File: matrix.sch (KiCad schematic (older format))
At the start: 139 parts

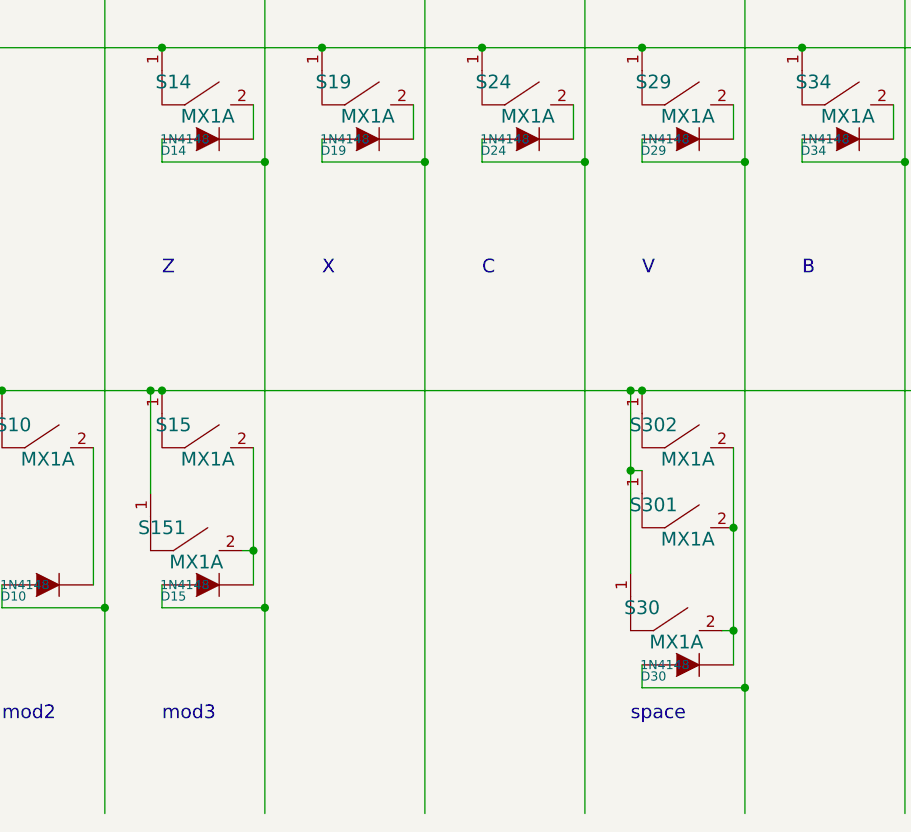
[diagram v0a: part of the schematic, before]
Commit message: Remove unnecessary related SWs to SW30
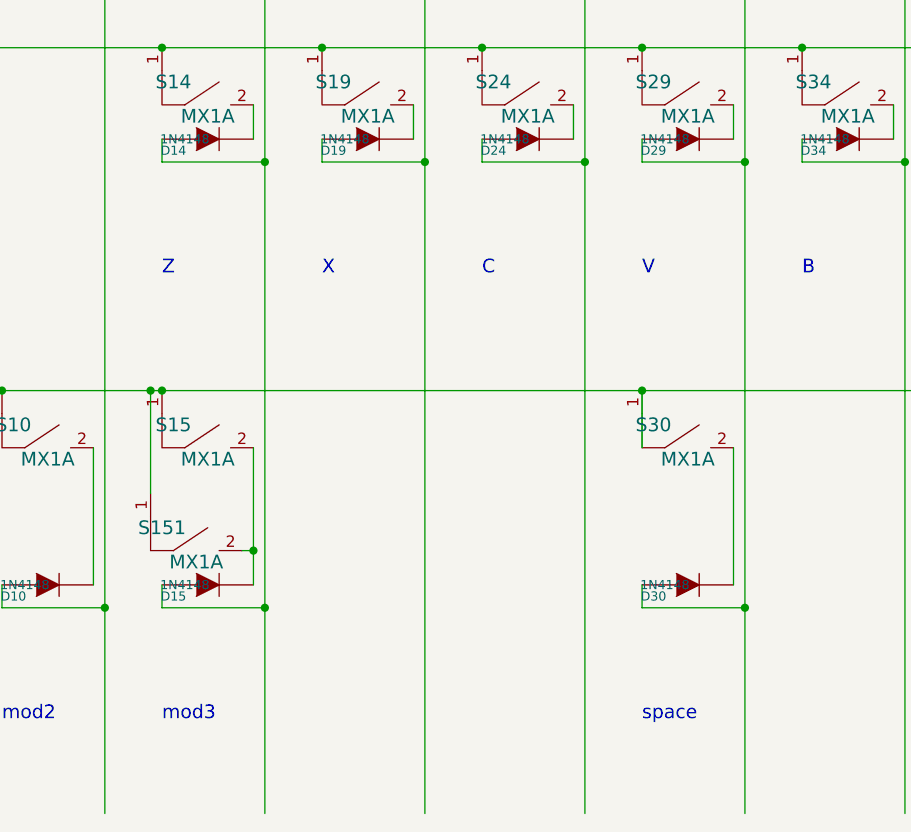
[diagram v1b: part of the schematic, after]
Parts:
- removed S301, S302: MX1A, mx1a:MX1A_no3d, symbol mx1a-simple:MX1A
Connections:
- wire segments 383 -> 377
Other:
- moved on the sheet: D30, S30
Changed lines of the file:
@@
-$EndComp
-$Comp
-L mx1a-simple:MX1A S301
-U 1 1 5040FAEC
-P 6850 8900
-F 0 "S301" H 6700 9150 60  0000 C CNN
-F 1 "MX1A" H 6850 9000 60  0000 C CNN
-F 2 "mx1a:MX1A_no3d" H 6850 8900 60  0001 C CNN
-F 3 "" H 6850 8900 60  0001 C CNN
-	1    6850 8900
-	1    0    0    -1
-$EndComp
-$Comp
-L mx1a-simple:MX1A S302
-U 1 1 5040FAF4
-P 6850 8550
-F 0 "S302" H 6700 8800 60  0000 C CNN
-F 1 "MX1A" H 6850 8650 60  0000 C CNN
-F 2 "mx1a:MX1A_no3d" H 6850 8550 60  0001 C CNN
-F 3 "" H 6850 8550 60  0001 C CNN
-	1    6850 8550
-	1    0    0    -1
 $EndComp
 $Comp
@@
 L mx1a-simple:MX1A S30
 U 1 1 5040DF35
-P 6800 9350
-F 0 "S30" H 6650 9600 60  0000 C CNN
-F 1 "MX1A" H 6800 9450 60  0000 C CNN
-F 2 "mx1a:MX1A" H 6800 9350 60  0001 C CNN
-F 3 "" H 6800 9350 60  0001 C CNN
-	1    6800 9350
+P 6850 8550
+F 0 "S30" H 6700 8800 60  0000 C CNN
+F 1 "MX1A" H 6850 8650 60  0000 C CNN
+F 2 "mx1a:MX1A" H 6850 8550 60  0001 C CNN
+F 3 "" H 6850 8550 60  0001 C CNN
+	1    6850 8550
 	1    0    0    -1
 $EndComp
@@
 L device:DIODE D30
 U 1 1 506B5D8C
-P 6850 9350
-F 0 "D30" H 6700 9300 40  0000 C CNN
-F 1 "1N4148" H 6750 9350 40  0000 C CNN
-F 2 "0805:0805D" H 6850 9350 60  0001 C CNN
-F 3 "" H 6850 9350 60  0001 C CNN
-F 4 "DC Components" H 4100 5050 60  0001 C CNN "Vendor"
-F 5 "CD4148WS(0805C)" H 4100 5050 60  0001 C CNN "Product"
-F 6 "TME" H 4100 5050 60  0001 C CNN "Supplier"
-F 7 "1N4148-0805" H 4100 5050 60  0001 C CNN "Supplier Symbol"
-	1    6850 9350
+P 6850 9000
+F 0 "D30" H 6700 8950 40  0000 C CNN
+F 1 "1N4148" H 6750 9000 40  0000 C CNN
+F 2 "0805:0805D" H 6850 9000 60  0001 C CNN
+F 3 "" H 6850 9000 60  0001 C CNN
+F 4 "DC Components" H 4100 4700 60  0001 C CNN "Vendor"
+F 5 "CD4148WS(0805C)" H 4100 4700 60  0001 C CNN "Product"
+F 6 "TME" H 4100 4700 60  0001 C CNN "Supplier"
+F 7 "1N4148-0805" H 4100 4700 60  0001 C CNN "Supplier Symbol"
+	1    6850 9000
 	1    0    0    -1
 $EndComp
@@
 Text Notes 4550 9600 0    60   ~ 0
 mod3
-Text Notes 6600 9600 0    60   ~ 0
-space
 Text Notes 10100 9600 0    60   ~ 0
 mod4
@@
 	11250 8400 11250 8700
 Wire Wire Line
-	7050 8400 7050 8750
-Wire Wire Line
 	12650 8400 12650 8850
 Wire Wire Line
@@
 Connection ~ 12200 5150
 Wire Wire Line
-	6600 8150 6600 8500
-Connection ~ 6600 8150
-Wire Wire Line
 	10550 8850 10500 8850
 Wire Wire Line
@@
 Wire Wire Line
 	12650 8850 12600 8850
-Wire Wire Line
-	7050 9200 7000 9200
 Wire Wire Line
 	12200 6650 12200 7100
@@
 Connection ~ 5950 5150
 Connection ~ 5950 6650
-Connection ~ 6650 8150
 Connection ~ 8750 2950
 Connection ~ 8050 2950
@@
 Wire Wire Line
 	4550 9000 4550 9100
-Wire Wire Line
-	6650 9350 6650 9450
-Wire Wire Line
-	6650 9450 7100 9450
 Connection ~ 12650 8850
 Connection ~ 11950 8850
 Connection ~ 10550 8850
 Connection ~ 11250 9150
-Connection ~ 7050 9200
 Wire Wire Line
 	3150 5550 3150 5650
@@
 Connection ~ 6400 7150
 Connection ~ 5700 7150
-Connection ~ 7100 9450
 Connection ~ 9200 3450
 Connection ~ 9900 3450
@@
 Wire Wire Line
 	12250 3450 12250 3350
-Connection ~ 7050 8750
-Wire Wire Line
-	6650 8500 6600 8500
-Connection ~ 6600 8500
 Wire Wire Line
 	12600 7350 12650 7350
@@
 	10150 8150 10800 8150
 Wire Wire Line
-	4550 8150 6600 8150
-Wire Wire Line
 	12250 6650 13250 6650
 Wire Wire Line
@@
 	12200 5150 12250 5150
 Wire Wire Line
-	6600 8150 6650 8150
-Wire Wire Line
 	12200 6650 12250 6650
 Wire Wire Line
@@
 	11250 9150 11250 9300
 Wire Wire Line
-	7050 9200 7050 9350
-Wire Wire Line
 	3600 3450 3600 4650
 Wire Wire Line
@@
 	7800 7150 7800 10000
 Wire Wire Line
-	7100 7150 7100 9450
-Wire Wire Line
 	6400 7150 6400 10000
 Wire Wire Line
 	5700 7150 5700 10000
 Wire Wire Line
-	7100 9450 7100 10000
-Wire Wire Line
 	9200 3450 9200 4650
 Wire Wire Line
@@
 	12650 7500 12650 7650
 Wire Wire Line
-	7050 8750 7050 9200
-Wire Wire Line
-	6600 8500 6600 8950
-Wire Wire Line
 	12650 7350 12650 7500
 Wire Wire Line
 	12200 7100 12200 7250
-Wire Wire Line
-	6650 8150 10100 8150
 Wire Wire Line
 	9900 7150 9900 10000
@@
 Wire Wire Line
 	3600 5650 3600 7450
+Wire Wire Line
+	7050 8400 7050 9000
+Wire Wire Line
+	6650 8150 6650 8400
+Wire Wire Line
+	7100 7150 7100 9100
+Connection ~ 6650 8150
+Wire Wire Line
+	6650 8150 10100 8150
+Wire Wire Line
+	4550 8150 6650 8150
+Wire Wire Line
+	6650 9000 6650 9100
+Wire Wire Line
+	6650 9100 7100 9100
+Connection ~ 7100 9100
+Wire Wire Line
+	7100 9100 7100 10000
+Text Notes 6650 9600 0    60   ~ 0
+space
 $EndSCHEMATC

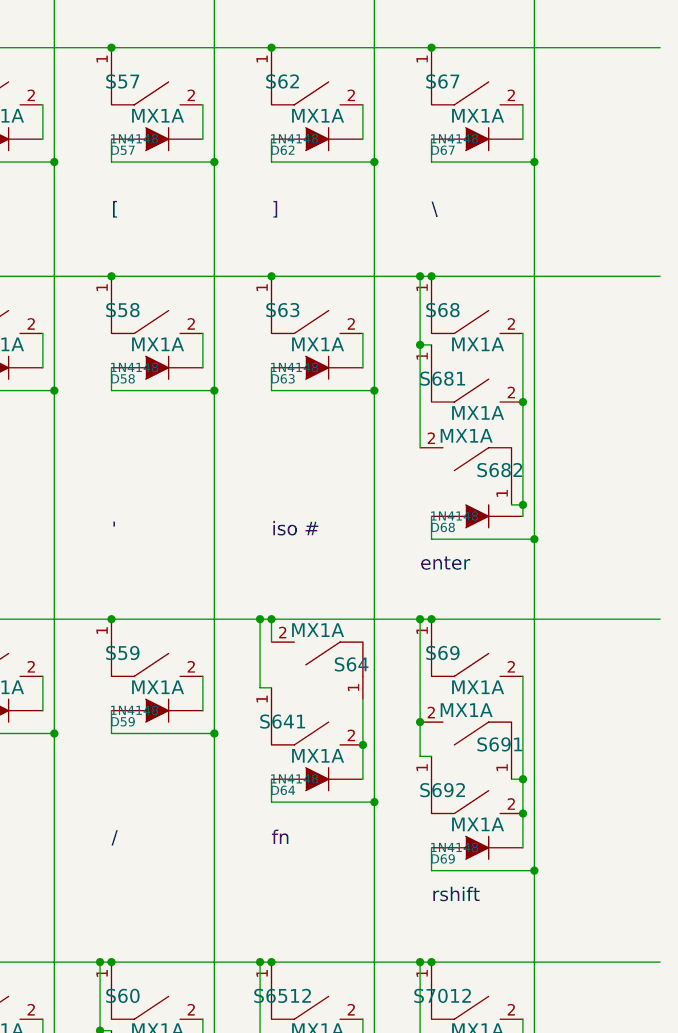
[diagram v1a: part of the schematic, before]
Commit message: Remove unnecessary SWs next to enter
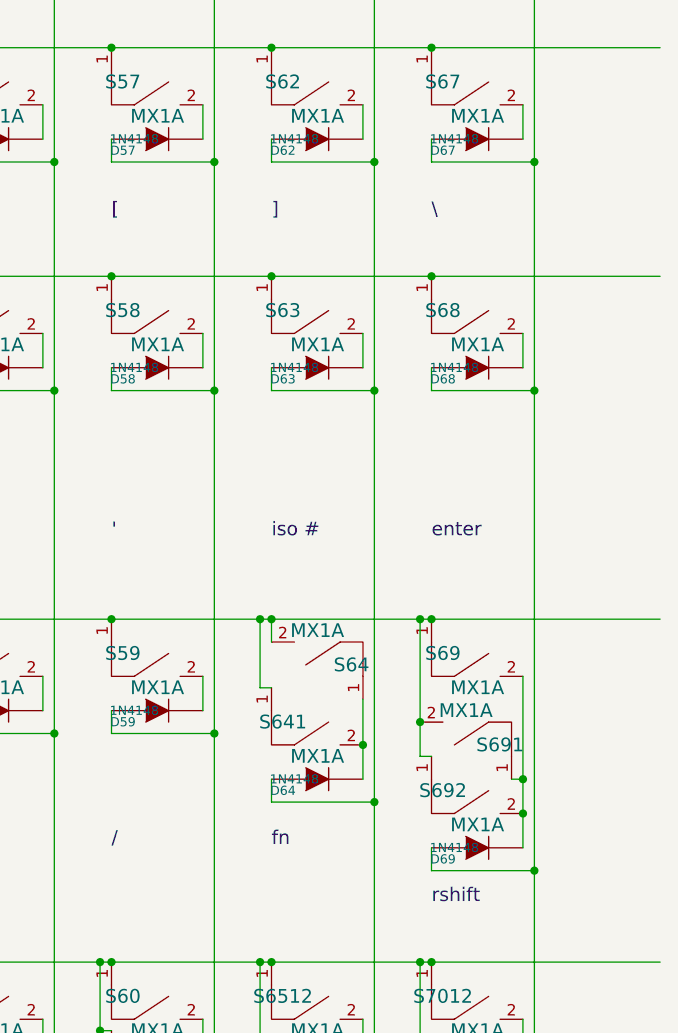
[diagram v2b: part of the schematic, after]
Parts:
- removed S681, S682: MX1A, mx1a:MX1A_no3d, symbol mx1a-simple:MX1A
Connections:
- wire segments 377 -> 370
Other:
- moved on the sheet: D68
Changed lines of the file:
@@
-$EndComp
-$Comp
-L mx1a-simple:MX1A S681
-U 1 1 5040E5A6
-P 12450 5850
-F 0 "S681" H 12300 6100 60  0000 C CNN
-F 1 "MX1A" H 12450 5950 60  0000 C CNN
-F 2 "mx1a:MX1A_no3d" H 12450 5850 60  0001 C CNN
-F 3 "" H 12450 5850 60  0001 C CNN
-	1    12450 5850
-	1    0    0    -1
 $EndComp
 $Comp
@@
 L device:DIODE D68
 U 1 1 506B5A16
-P 12450 6200
-F 0 "D68" H 12300 6150 40  0000 C CNN
-F 1 "1N4148" H 12350 6200 40  0000 C CNN
-F 2 "0805:0805D" H 12450 6200 60  0001 C CNN
-F 3 "" H 12450 6200 60  0001 C CNN
-F 4 "DC Components" H 5300 4700 60  0001 C CNN "Vendor"
-F 5 "CD4148WS(0805C)" H 5300 4700 60  0001 C CNN "Product"
-F 6 "TME" H 5300 4700 60  0001 C CNN "Supplier"
-F 7 "1N4148-0805" H 5300 4700 60  0001 C CNN "Supplier Symbol"
-	1    12450 6200
+P 12450 5550
+F 0 "D68" H 12300 5500 40  0000 C CNN
+F 1 "1N4148" H 12350 5550 40  0000 C CNN
+F 2 "0805:0805D" H 12450 5550 60  0001 C CNN
+F 3 "" H 12450 5550 60  0001 C CNN
+F 4 "DC Components" H 5300 4050 60  0001 C CNN "Vendor"
+F 5 "CD4148WS(0805C)" H 5300 4050 60  0001 C CNN "Product"
+F 6 "TME" H 5300 4050 60  0001 C CNN "Supplier"
+F 7 "1N4148-0805" H 5300 4050 60  0001 C CNN "Supplier Symbol"
+	1    12450 5550
 	1    0    0    -1
 $EndComp
@@
 	1    3350 5550
 	1    0    0    -1
-$EndComp
-$Comp
-L mx1a-simple:MX1A S682
-U 1 1 50871329
-P 12400 5750
-F 0 "S682" H 12250 6000 60  0000 C CNN
-F 1 "MX1A" H 12400 5850 60  0000 C CNN
-F 2 "mx1a:MX1A_no3d" H 12400 5750 60  0001 C CNN
-F 3 "" H 12400 5750 60  0001 C CNN
-	1    12400 5750
-	-1   0    0    1
 $EndComp
 $Comp
@@
 Text Notes 11550 6300 0    60   ~ 0
 iso #
-Text Notes 12200 6450 0    60   ~ 0
+Text Notes 12250 6300 0    60   ~ 0
 enter
 Text Notes 4550 7650 0    60   ~ 0
@@
 	11950 7000 11950 7200
 Wire Wire Line
-	12200 5150 12200 5450
-Wire Wire Line
-	12200 5450 12250 5450
-Connection ~ 12200 5150
-Wire Wire Line
 	10550 8850 10500 8850
 Wire Wire Line
@@
 	10150 9100 10600 9100
 Wire Wire Line
-	12250 6300 12700 6300
+	12250 5650 12700 5650
 Wire Wire Line
 	11550 5550 11550 5650
@@
 Connection ~ 11300 5650
 Connection ~ 12000 5650
-Connection ~ 12700 6300
 Connection ~ 12700 9100
 Connection ~ 12700 7750
@@
 Connection ~ 9900 7150
 Connection ~ 9200 7150
-Wire Wire Line
-	12650 5400 12650 5700
-Connection ~ 12650 5700
 Connection ~ 11950 7200
 Connection ~ 9450 5150
 Connection ~ 9450 4150
 Connection ~ 9450 2950
-Wire Wire Line
-	12250 6300 12250 6200
-Connection ~ 12200 5450
-Wire Wire Line
-	12600 6150 12650 6150
-Connection ~ 12650 6150
 Connection ~ 12650 7500
 Wire Wire Line
@@
 	10850 5150 11550 5150
 Wire Wire Line
-	11550 5150 12200 5150
-Wire Wire Line
 	12250 5150 13250 5150
 Wire Wire Line
@@
 	11500 6650 11550 6650
 Wire Wire Line
-	12200 5150 12250 5150
-Wire Wire Line
 	12200 6650 12250 6650
 Wire Wire Line
@@
 	12000 3450 12000 4650
 Wire Wire Line
-	12700 4650 12700 6300
+	12700 4650 12700 5650
 Wire Wire Line
 	12000 4650 12000 5650
@@
 	12000 5650 12000 7450
 Wire Wire Line
-	12700 6300 12700 7750
-Wire Wire Line
 	12700 9100 12700 10000
 Wire Wire Line
@@
 	9200 7150 9200 10000
 Wire Wire Line
-	12650 5700 12650 6150
-Wire Wire Line
 	11950 7200 11950 7350
 Wire Wire Line
@@
 Wire Wire Line
 	9450 2950 10150 2950
-Wire Wire Line
-	12200 5450 12200 5900
-Wire Wire Line
-	12650 6150 12650 6200
 Wire Wire Line
 	12650 7500 12650 7650
@@
 Text Notes 6650 9600 0    60   ~ 0
 space
+Wire Wire Line
+	12650 5400 12650 5550
+Wire Wire Line
+	11550 5150 12250 5150
+Connection ~ 12700 5650
+Wire Wire Line
+	12700 5650 12700 7750
+Wire Wire Line
+	12250 5550 12250 5650
 $EndSCHEMATC
